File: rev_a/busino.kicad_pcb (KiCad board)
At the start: 2 copper layers, 62 parts, among them J1 TERMINATE_JUMPER, J2 LED_JUMPER, SW1 2_LEAD_PUSH_BUTTON, U1 LM2940CT-5.0, U2 MCP2562, U3 LM1117T-3.3, U4 74x06, U5 ATMEGA324_DIP40, X1 16MHz, X2 OSHW_LOGO

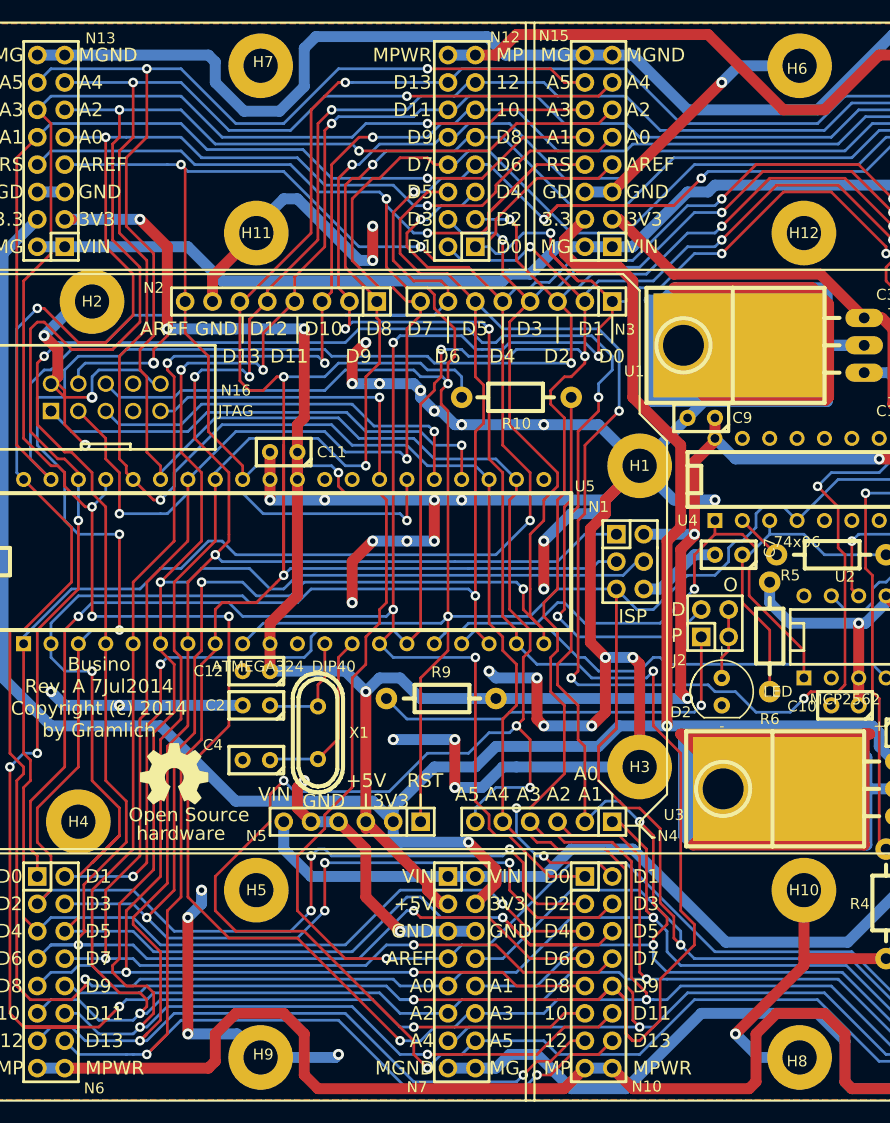
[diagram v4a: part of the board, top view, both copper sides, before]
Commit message: Minor polishing.  Noticed that mounting holes were masked when they should not be masked.
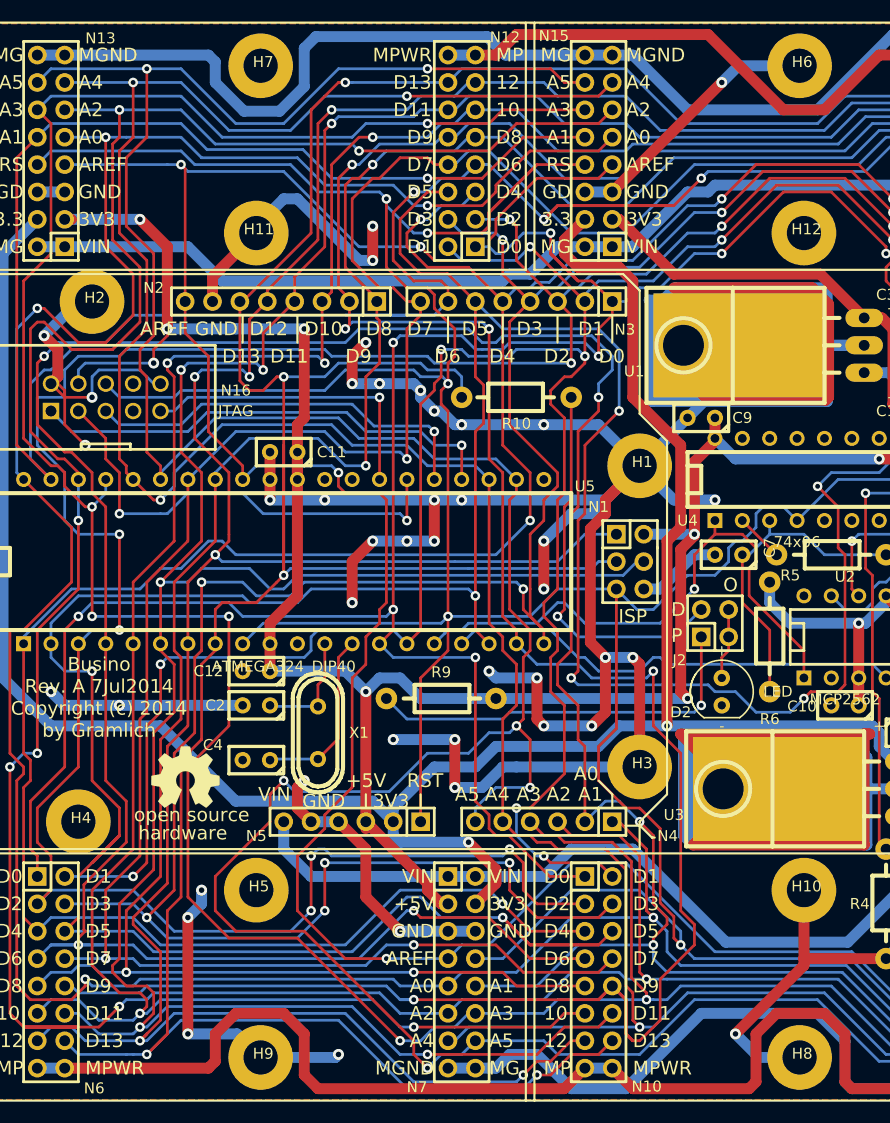
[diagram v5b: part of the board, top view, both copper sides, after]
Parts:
- moved X2 1.09 mm to (44.2, 96.2)
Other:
- board text added: "open source"
- board text removed: "Open Source"

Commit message: More work on the ground plane.
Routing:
- net GND: track 641.1 -> 943.1 mm, vias 42 -> 61
- net Net-(N8-Pad6): track 31.7 -> 16.4 mm, vias 1 -> 0
- net /Arduino Shield/D6: track 262.8 -> 253.4 mm
- net Net-(C6-Pad1): track 64.3 -> 72.4 mm, vias 1 -> 2
- net +5V: track 318.5 -> 320.5 mm
- net /Arduino Shield/D5: track 338.5 -> 340.3 mm
- net Net-(C7-Pad1): track 30.6 -> 32.0 mm, vias 0 -> 1
- net /Arduino Shield/~RESET: track 358.1 -> 359.2 mm
- net /Arduino Shield/A4: track 251.3 -> 252.3 mm
- net /Arduino Shield/D1: track 230.9 -> 230.3 mm
- net +3.3V: vias 3 -> 4
- net (no net): vias 1 -> 0
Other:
- board outline added: 100 x 100 mm
- board text added: "1"
